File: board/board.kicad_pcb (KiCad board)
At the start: 2 copper layers, 195 x 160 mm, 235 parts, among them J1 Conn_02x03_Odd_Even, J3 RPi_GPIO, SW1 SW_Push, SW2 SW_Push, SW3 SW_Push, SW4 SW_Push, U1 74HC238, U10 A3144, U11 A3144, U12 A3144, U13 A3144, U14 A3144, U15 A3144, U16 A3144, U17 A3144, U18 A3144, U19 A3144, U2 74LS151, U20 A3144, U21 A3144, U22 A3144, U23 A3144, U24 A3144, U25 A3144, U26 A3144, U27 A3144, U28 A3144, U29 A3144, U3 A3144, U30 A3144, U31 A3144, U32 A3144, U33 A3144, U34 A3144, U35 A3144, U36 A3144, U37 A3144, U38 A3144, U39 A3144, U4 A3144, U40 A3144, U41 A3144, U42 A3144, U43 A3144, U44 A3144, U45 A3144, U46 A3144, U47 A3144, U48 A3144, U49 A3144, U5 A3144, U50 A3144, U51 A3144, U52 A3144, U53 A3144, U54 A3144, U55 A3144, U56 A3144, U57 A3144, U58 A3144, U59 A3144, U6 A3144, U60 A3144, U61 A3144, U62 A3144, U63 A3144, U64 A3144, U65 A3144, U66 A3144, U7 A3144, U8 A3144, U9 A3144

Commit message: PCB: Minor changes
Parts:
- removed REF**: rpi_zero_outline, board:rpi_zero_outline
- C1: footprint Capacitor_THT:C_Radial_D6.3mm_H11.0mm_P2.50mm -> Capacitor_SMD:C_0805_2012Metric_Pad1.18x1.45mm_HandSolder
- J1: value Conn_02x03_Odd_Even -> Conn_01x02_Female; footprint Connector_PinHeader_2.54mm:PinHeader_2x03_P2.54mm_Vertical -> Connector_JST:JST_XH_B2B-XH-A_1x02_P2.50mm_Vertical
- moved C1 34.1 mm to (232.2, 206.7), turned to 270 degrees
- moved J1 1.84 mm to (237.2, 205.6), turned to 0 degrees
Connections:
- J3 pad 1: Net-(J3-Pad1) -> (no net)
- J3 pad 14: Net-(J3-Pad14) -> (no net)
- J3 pad 16: Net-(J3-Pad16) -> (no net)
- J3 pad 17: Net-(J3-Pad17) -> (no net)
- J3 pad 20: Net-(J3-Pad20) -> (no net)
- J3 pad 25: Net-(J3-Pad25) -> (no net)
- J3 pad 27: Net-(J3-Pad27) -> (no net)
- J3 pad 28: Net-(J3-Pad28) -> (no net)
- J3 pad 29: Net-(J3-Pad29) -> (no net)
- J3 pad 30: Net-(J3-Pad30) -> (no net)
- J3 pad 34: Net-(J3-Pad34) -> (no net)
- J3 pad 4: Net-(J3-Pad4) -> (no net)
- J3 pad 6: Net-(J3-Pad6) -> (no net)
- J3 pad 9: Net-(J3-Pad9) -> (no net)
- U2 pad 6: Net-(U2-Pad6) -> (no net)
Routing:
- net GND: track 0.00 -> 14.0 mm

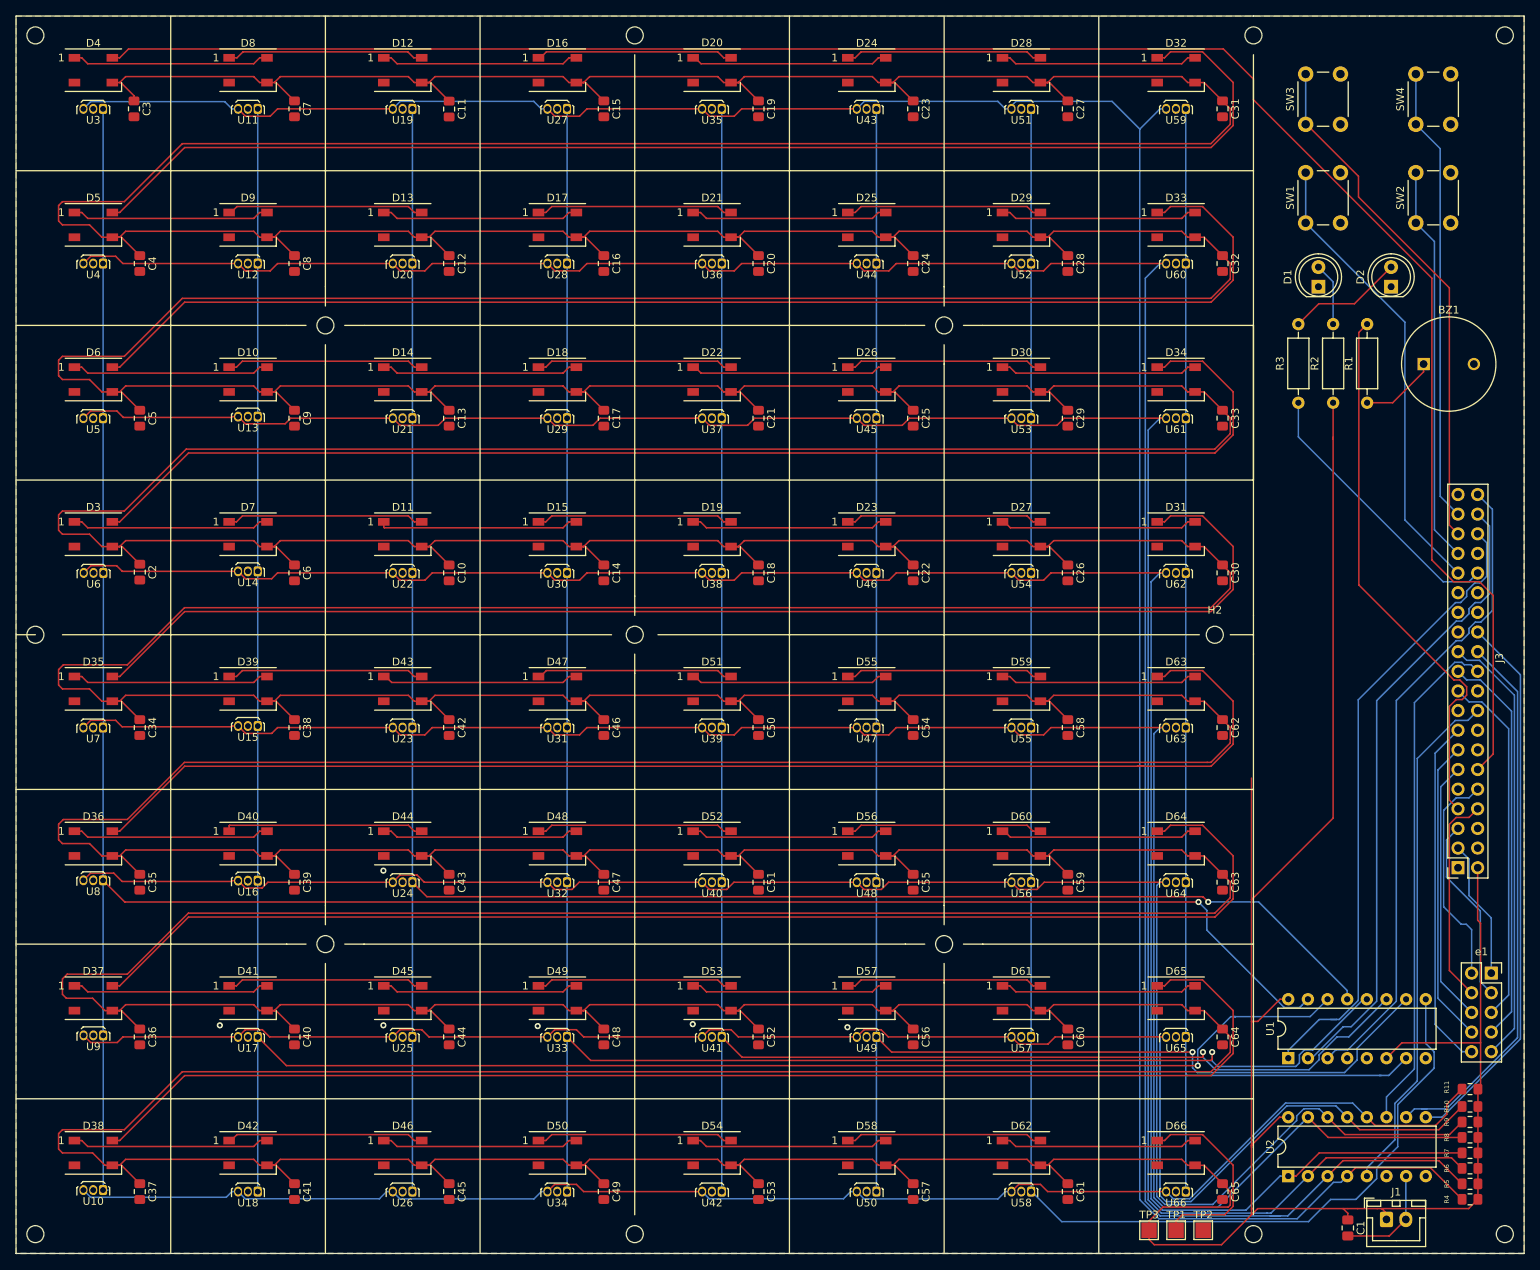
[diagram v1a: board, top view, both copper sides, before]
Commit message: Folder reorganized: board
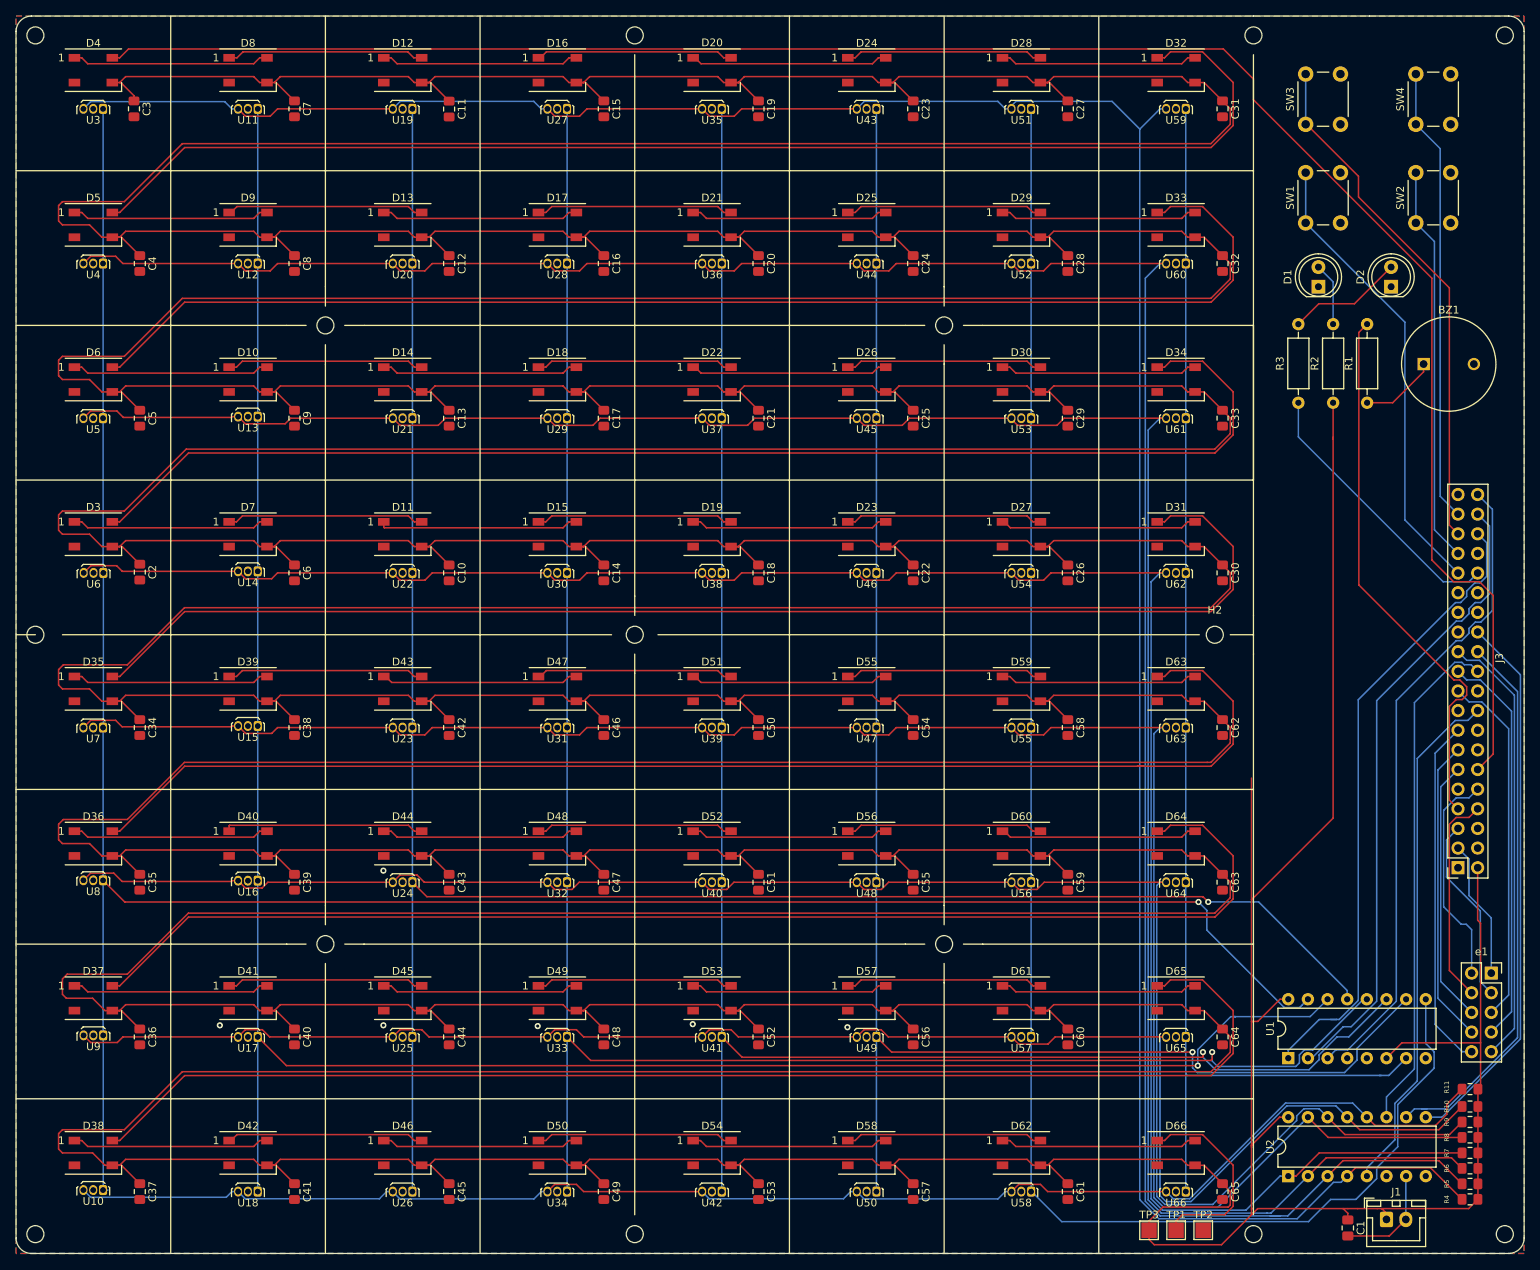
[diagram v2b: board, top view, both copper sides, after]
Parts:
- J3: footprint board:raspberry_pi_socket -> Board:raspberry_pi_socket
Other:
- outline, holes or cut-outs redrawn
